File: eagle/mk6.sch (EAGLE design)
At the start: 13 parts, among them IC2 78L05F, J1 AVR_SPI_PROG_3X2PTH, U1 ATTINY85-20SU

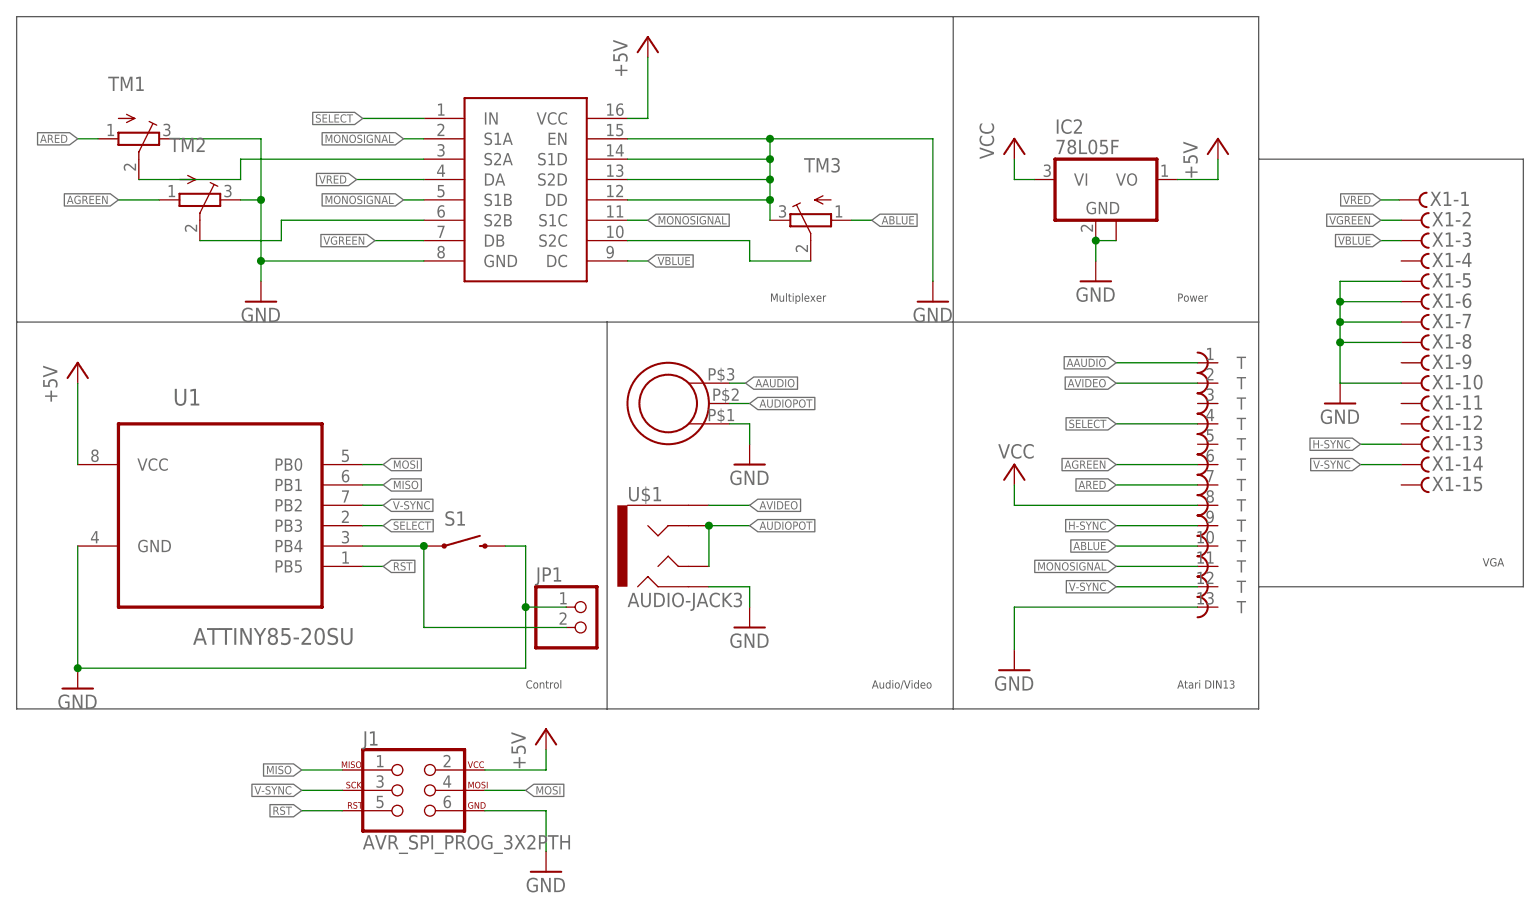
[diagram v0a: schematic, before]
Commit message: v1.4. Added AG-pad, different button than 1.3b
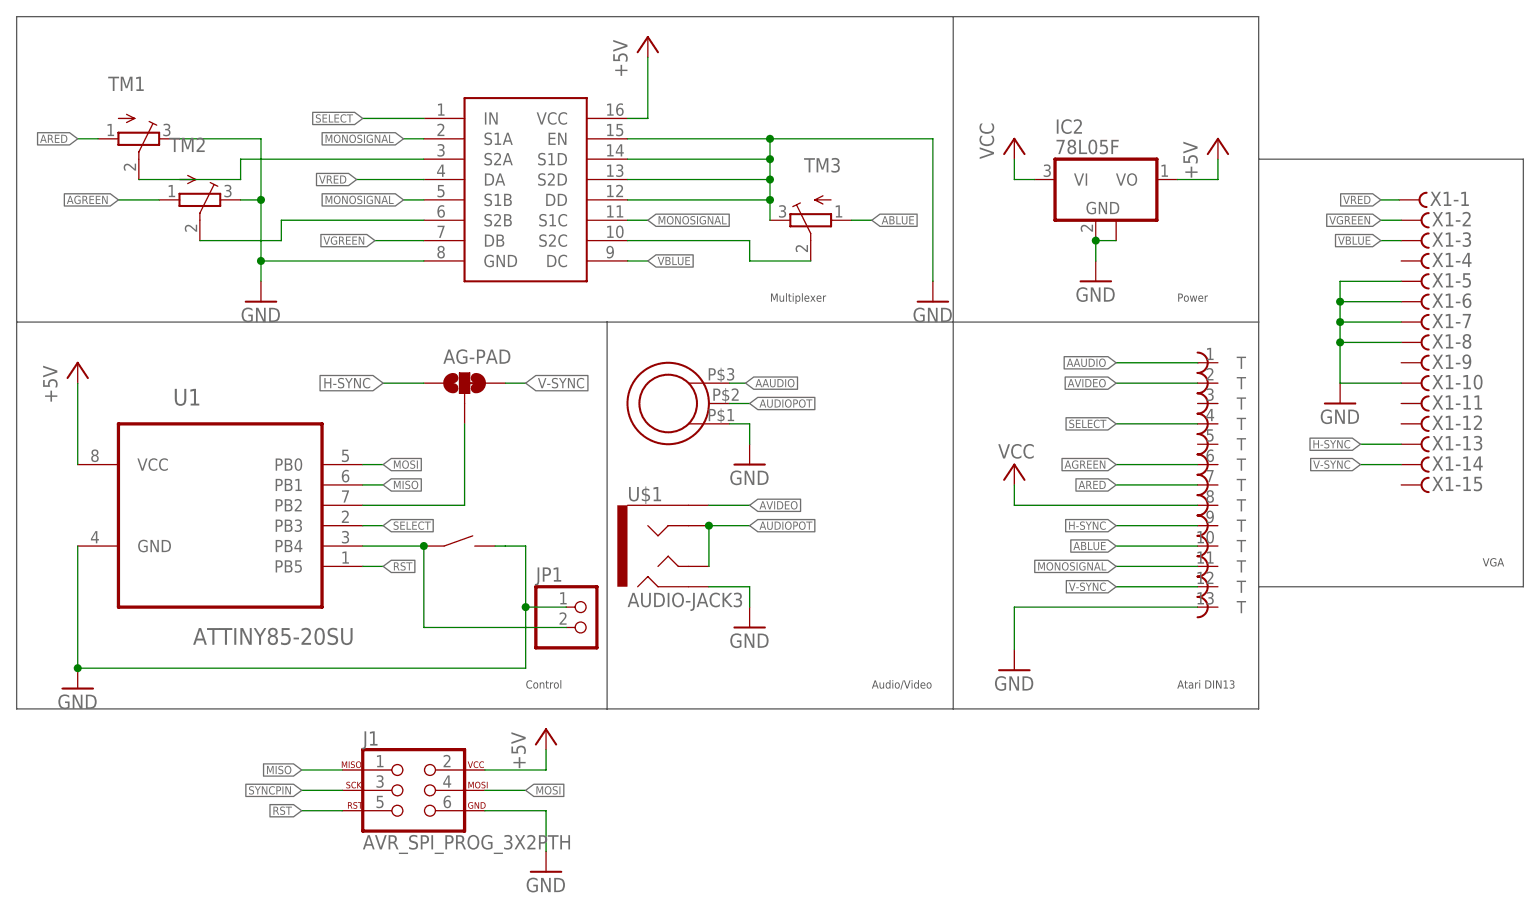
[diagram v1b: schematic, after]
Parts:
- removed S1: SWITCH-MOMENTARY-2TACTILE-SWITCH-SMD-RIGHT-ANGLE, SparkFun-Electromechanical:SWITCH-MOMENTARY-2TACTILE-SWITCH-SMD-RIGHT-ANGLE
- added AG-PAD: JUMPER-SMT_3_1-NC_TRACE_SILK, SparkFun-Jumpers:JUMPER-SMT_3_1-NC_TRACE_SILK
- added S2: K2-1823SA, ube:K2-1823SA
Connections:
- new net SYNCPIN: AG-PAD.2, J1.3, U1.PB2
- net GND: now also S2.2; no longer S1.2
- net H-SYNC: now also AG-PAD.1
- net N$6: now also S2.1; no longer S1.1
- net V-SYNC: now also AG-PAD.3; no longer J1.3, U1.PB2
